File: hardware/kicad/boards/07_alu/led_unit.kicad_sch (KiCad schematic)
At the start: 27 parts

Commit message: checkpoint: most recent 16b cell: ~120mm by 120mm
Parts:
- removed D5, D6, D7, D8: LED, LED_SMD:LED_0805_2012Metric, symbol Device:LED
- removed R5, R6, R7, R8: 330, Resistor_SMD:R_0603_1608Metric, symbol Device:R
- added D17, D18, D19, D20, D21, D22, D23, D24, D25, D26, D27, D28, D29, D30, D31, D32: LED, LED_SMD:LED_0805_2012Metric, symbol Device:LED
- added R16, R17, R18, R19, R20, R21, R22, R23, R24, R25, R26, R27, R28, R29, R30, R31: 330, Resistor_SMD:R_0603_1608Metric, symbol Device:R
- D16, D3: footprint LED_THT:LED_D5.0mm -> LED_SMD:LED_0805_2012Metric
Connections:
- net GND: now also D17.1 (K), D18.1 (K), D19.1 (K), D20.1 (K), D21.1 (K), D22.1 (K), D23.1 (K), D24.1 (K), D25.1 (K), D26.1 (K), D27.1 (K), D28.1 (K), D29.1 (K), D30.1 (K), D31.1 (K), D32.1 (K)
- new net: D18.2 (A), R17.2
- new net: D26.2 (A), R25.2
- new net: D28.2 (A), R27.2
- new net: D27.2 (A), R26.2
- new net: D21.2 (A), R20.2
- new net: D20.2 (A), R19.2
- new net: D29.2 (A), R28.2
- new net: D24.2 (A), R23.2
- new net: D19.2 (A), R18.2
- new net: D22.2 (A), R21.2
- new net: D17.2 (A), R16.2
- new net: D30.2 (A), R29.2
- new net: D32.2 (A), R31.2
- new net: D23.2 (A), R22.2
- new net: D31.2 (A), R30.2
- new net: D25.2 (A), R24.2
- new net ALU_OPCODE_X0: R16.1
- new net ALU_OPCODE_X1: R17.1
- new net ALU_OPCODE_X2: R18.1
- new net ALU_OPCODE_X3: R19.1
- new net ALU_OPCODE_X4: R20.1
- new net ALU_OPCODE_X5: R21.1
- new net ALU_OPCODE_X6: R22.1
- new net ALU_OPCODE_X7: R23.1
- new net ALU_OPCODE_Y0: R24.1
- new net ALU_OPCODE_Y1: R25.1
- new net ALU_OPCODE_Y2: R26.1
- new net ALU_OPCODE_Y3: R27.1
- new net ALU_OPCODE_Y4: R28.1
- new net ALU_OPCODE_Y5: R29.1
- new net ALU_OPCODE_Y6: R30.1
- new net ALU_OPCODE_Y7: R31.1
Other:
- moved on the sheet: D9, R9

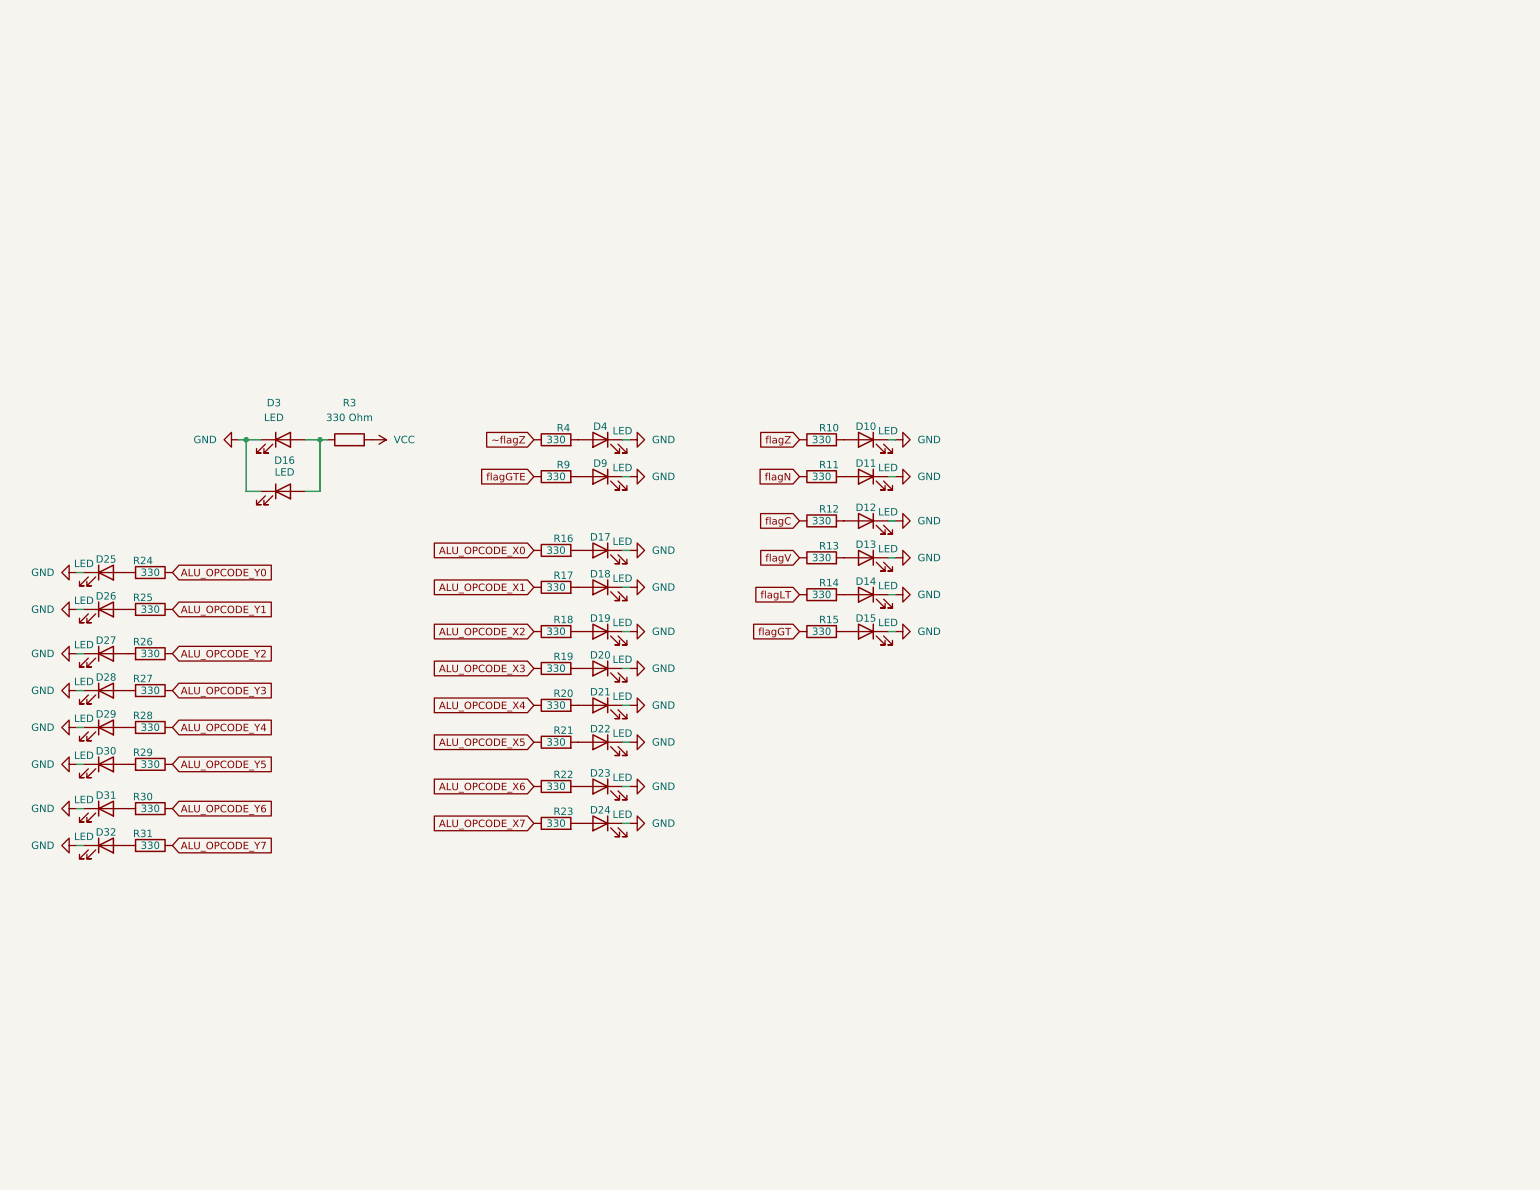
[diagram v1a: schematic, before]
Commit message: fix: resolved kicad erc tests to 0
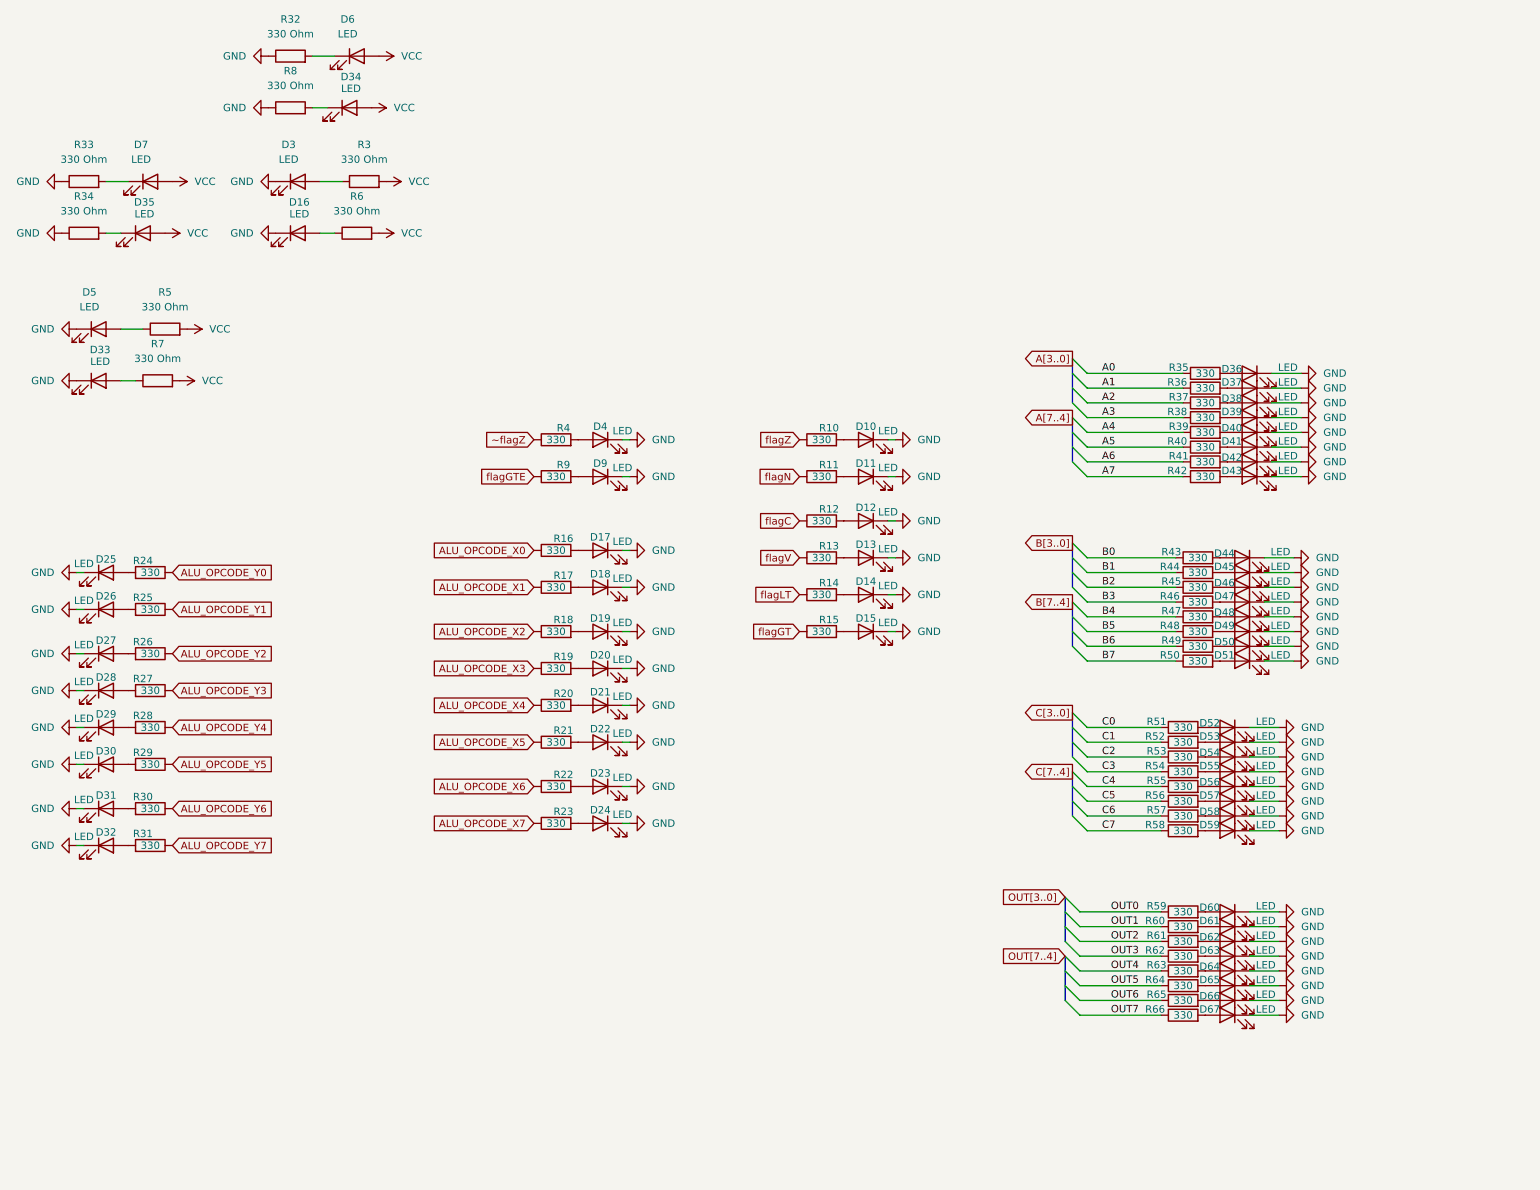
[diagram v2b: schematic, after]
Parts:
- added D33, D34, D35, D36, D37, D38, D39, D40, D41, D42, D43, D44, D45, D46, D47, D48, D49, D5, D50, D51, D52, D53, D54, D55, D56, D57, D58, D59, D6, D60, D61, D62, D63, D64, D65, D66, D67, D7: LED, LED_SMD:LED_0805_2012Metric, symbol Device:LED
- added R32, R33, R34, R5, R6, R7, R8: 330 Ohm, Resistor_SMD:R_0603_1608Metric, symbol Device:R
- added R35, R36, R37, R38, R39, R40, R41, R42, R43, R44, R45, R46, R47, R48, R49, R50, R51, R52, R53, R54, R55, R56, R57, R58, R59, R60, R61, R62, R63, R64, R65, R66: 330, Resistor_SMD:R_0603_1608Metric, symbol Device:R
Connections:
- net GND: now also D33.1 (K), D36.1 (K), D37.1 (K), D38.1 (K), D39.1 (K), D40.1 (K), D41.1 (K), D42.1 (K), D43.1 (K), D44.1 (K), D45.1 (K), D46.1 (K), D47.1 (K), D48.1 (K), D49.1 (K), D5.1 (K), D50.1 (K), D51.1 (K), D52.1 (K), D53.1 (K), D54.1 (K), D55.1 (K), D56.1 (K), D57.1 (K), D58.1 (K), D59.1 (K), D60.1 (K), D61.1 (K), D62.1 (K), D63.1 (K), D64.1 (K), D65.1 (K), D66.1 (K), D67.1 (K), R32.1, R33.1, R34.1, R8.1
- net VCC: now also D34.2 (A), D35.2 (A), D6.2 (A), D7.2 (A), R5.2, R6.2, R7.2
- net at D3.2 (A), R3.1: no longer D16.2 (A)
- new net: D53.2 (A), R52.2
- new net: D44.2 (A), R43.2
- new net: D52.2 (A), R51.2
- new net: D36.2 (A), R35.2
- new net: D61.2 (A), R60.2
- new net: D67.2 (A), R66.2
- new net: D59.2 (A), R58.2
- new net: D34.1 (K), R8.2
- new net: D63.2 (A), R62.2
- new net: D42.2 (A), R41.2
- new net: D7.1 (K), R33.2
- new net: D37.2 (A), R36.2
- new net: D55.2 (A), R54.2
- new net: D48.2 (A), R47.2
- new net: D60.2 (A), R59.2
- new net: D45.2 (A), R44.2
- new net: D43.2 (A), R42.2
- new net: D33.2 (A), R7.1
- new net: D46.2 (A), R45.2
- new net: D5.2 (A), R5.1
- new net: D6.1 (K), R32.2
- new net: D16.2 (A), R6.1
- new net: D56.2 (A), R55.2
- new net: D54.2 (A), R53.2
- new net: D39.2 (A), R38.2
- new net: D47.2 (A), R46.2
- new net: D49.2 (A), R48.2
- new net: D40.2 (A), R39.2
- new net: D51.2 (A), R50.2
- new net: D50.2 (A), R49.2
- new net: D62.2 (A), R61.2
- new net: D65.2 (A), R64.2
- new net: D41.2 (A), R40.2
- new net: D38.2 (A), R37.2
- new net: D57.2 (A), R56.2
- new net: D58.2 (A), R57.2
- new net: D66.2 (A), R65.2
- new net: D35.1 (K), R34.2
- new net: D64.2 (A), R63.2
- new net A0: R35.1
- new net A1: R36.1
- new net A2: R37.1
- new net A3: R38.1
- new net A4: R39.1
- new net A5: R40.1
- new net A6: R41.1
- new net A7: R42.1
- new net B0: R43.1
- new net B1: R44.1
- new net B2: R45.1
- new net B3: R46.1
- new net B4: R47.1
- new net B5: R48.1
- new net B6: R49.1
- new net B7: R50.1
- new net C0: R51.1
- new net C1: R52.1
- new net C2: R53.1
- new net C3: R54.1
- new net C4: R55.1
- new net C5: R56.1
- new net C6: R57.1
- new net C7: R58.1
- new net OUT0: R59.1
- new net OUT1: R60.1
- new net OUT2: R61.1
- new net OUT3: R62.1
- new net OUT4: R63.1
- new net OUT5: R64.1
- new net OUT6: R65.1
- new net OUT7: R66.1
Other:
- moved on the sheet: D16, D3, R3

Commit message: checkpoint: routed all but 60 traces
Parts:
- removed D34, D35, D5, D9: LED, LED_SMD:LED_0805_2012Metric, symbol Device:LED
- removed R5, R6, R8: 330 Ohm, Resistor_SMD:R_0603_1608Metric, symbol Device:R
- removed R9: 330, Resistor_SMD:R_0603_1608Metric, symbol Device:R
- R34: value 330 Ohm -> 330
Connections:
- net GND: no longer R34.1
- net flagGTE: now also R34.1
- net at D16.2 (A): now also R34.2

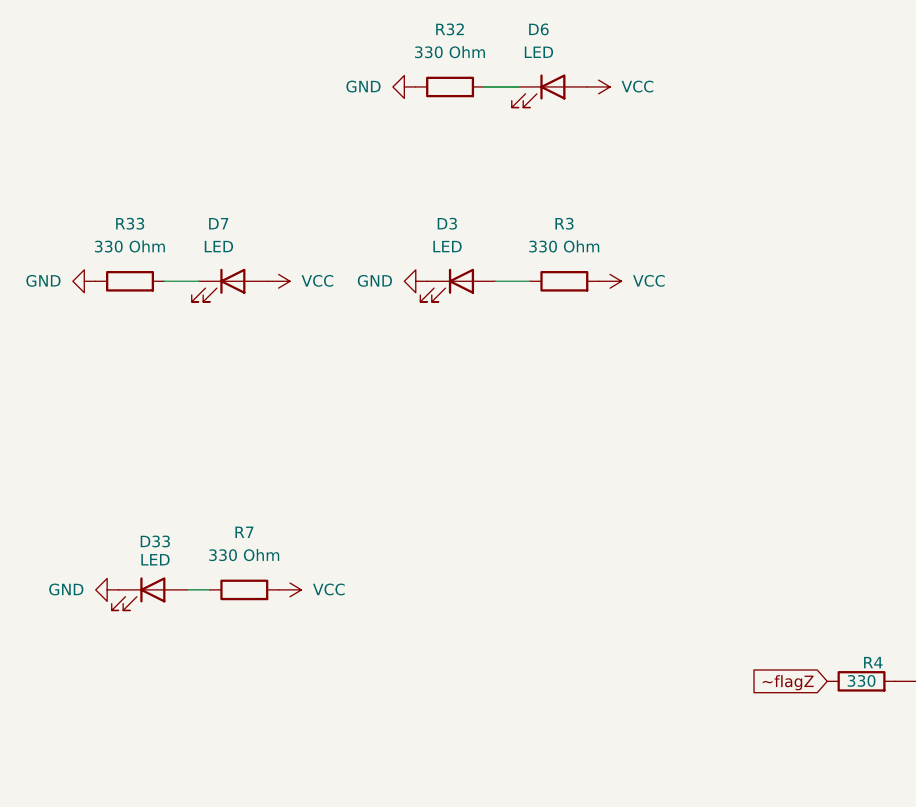
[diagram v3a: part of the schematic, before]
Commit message: feat: route 8b ALU slice and annotate pending final signoff 🎉🎉
Highlights:
- 0 ERC/DRC errors
- 0 Unrouted nets
- 2345 track segments
- 388 vias after cleanup
- 760 pads
- 18 core 74xx chips
- 7 flag 74xx chips

Pending additional confirmation of hardware-simulation faithfulness and fidelity.
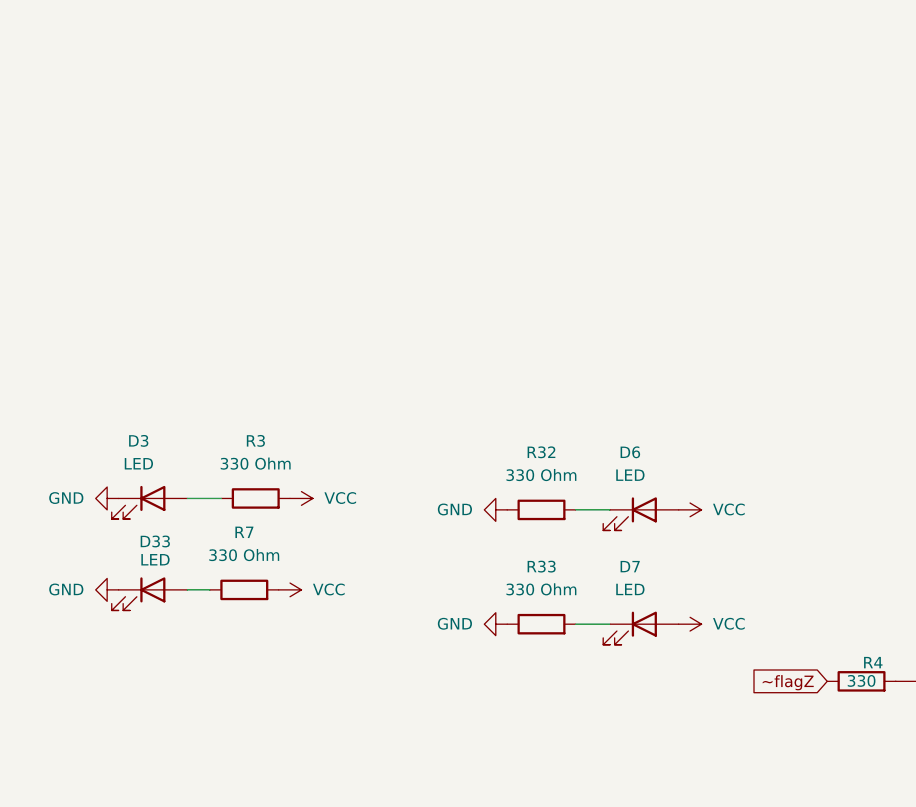
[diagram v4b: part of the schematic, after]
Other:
- moved on the sheet: D3, D6, D7, R3, R32, R33
